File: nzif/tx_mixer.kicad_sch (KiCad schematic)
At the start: 51 parts, among them U143 SN74CBT3125CPW, U144 SN74CBT3125CPW, U145 SN74CBT3125CPW, U146 SN74CBT3125CPW, U147 ADG918BRM, U148 ADA4807-2ACP, U149 ADA4807-2ACP, U150 ADA4807-2ACP, U151 ADG918BRM

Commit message: Digikey parts for rcv stages
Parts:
- C292, C293, C294, C295: Digikey Part # (none) -> 587-3258-1-ND
- C296, C297, C298, C299: Digikey Part # (none) -> 490-GCM31C5C1H104FA16LCT-ND
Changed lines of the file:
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@@
 			)
 		)
-		(property "Datasheet" "~"
+		(property "Datasheet" "https://search.murata.co.jp/Ceramy/image/img/A01X/G101/ENG/GCM31C5C1H104FA16-01.pdf"
 			(at 55.88 26.67 0)
 			(effects
@@
 			)
 		)
-		(property "Digikey Part #" ""
+		(property "Digikey Part #" "490-GCM31C5C1H104FA16LCT-ND"
 			(at 55.88 26.67 0)
 			(effects
@@
 			)
 		)
-		(property "Datasheet" "~"
+		(property "Datasheet" "https://search.murata.co.jp/Ceramy/image/img/A01X/G101/ENG/GCM31C5C1H104FA16-01.pdf"
 			(at 55.88 153.67 0)
 			(effects
@@
 			)
 		)
-		(property "Digikey Part #" ""
+		(property "Digikey Part #" "490-GCM31C5C1H104FA16LCT-ND"
 			(at 55.88 153.67 0)
 			(effects
@@
 			)
 		)
-		(property "Datasheet" "~"
+		(property "Datasheet" "https://search.murata.co.jp/Ceramy/image/img/A01X/G101/ENG/GCM31C5C1H104FA16-01.pdf"
 			(at 55.88 217.17 0)
 			(effects
@@
 			)
 		)
-		(property "Digikey Part #" ""
+		(property "Digikey Part #" "490-GCM31C5C1H104FA16LCT-ND"
 			(at 55.88 217.17 0)
 			(effects
@@
 			)
 		)
-		(property "Datasheet" "~"
+		(property "Datasheet" "https://mm.digikey.com/Volume0/opasdata/d220001/medias/docus/1231/LMK107BBJ106MALT_SS.pdf"
 			(at 46.99 90.17 0)
 			(effects
@@
 			)
 		)
-		(property "Digikey Part #" ""
+		(property "Digikey Part #" "587-3258-1-ND"
 			(at 46.99 90.17 0)
 			(effects
@@
 			)
 		)
-		(property "Datasheet" "~"
+		(property "Datasheet" "https://mm.digikey.com/Volume0/opasdata/d220001/medias/docus/1231/LMK107BBJ106MALT_SS.pdf"
 			(at 46.99 153.67 0)
 			(effects
@@
 			)
 		)
-		(property "Digikey Part #" ""
+		(property "Digikey Part #" "587-3258-1-ND"
 			(at 46.99 153.67 0)
 			(effects
@@
 			)
 		)
-		(property "Datasheet" "~"
+		(property "Datasheet" "https://search.murata.co.jp/Ceramy/image/img/A01X/G101/ENG/GCM31C5C1H104FA16-01.pdf"
 			(at 55.88 90.17 0)
 			(effects
@@
 			)
 		)
-		(property "Digikey Part #" ""
+		(property "Digikey Part #" "490-GCM31C5C1H104FA16LCT-ND"
 			(at 55.88 90.17 0)
 			(effects
@@
 			)
 		)
-		(property "Datasheet" "~"
+		(property "Datasheet" "https://mm.digikey.com/Volume0/opasdata/d220001/medias/docus/1231/LMK107BBJ106MALT_SS.pdf"
 			(at 46.99 217.17 0)
 			(effects
@@
 			)
 		)
-		(property "Digikey Part #" ""
+		(property "Digikey Part #" "587-3258-1-ND"
 			(at 46.99 217.17 0)
 			(effects
@@
 			)
 		)
-		(property "Datasheet" "~"
+		(property "Datasheet" "https://mm.digikey.com/Volume0/opasdata/d220001/medias/docus/1231/LMK107BBJ106MALT_SS.pdf"
 			(at 46.99 26.67 0)
 			(effects
@@
 			)
 		)
-		(property "Digikey Part #" ""
+		(property "Digikey Part #" "587-3258-1-ND"
 			(at 46.99 26.67 0)
 			(effects

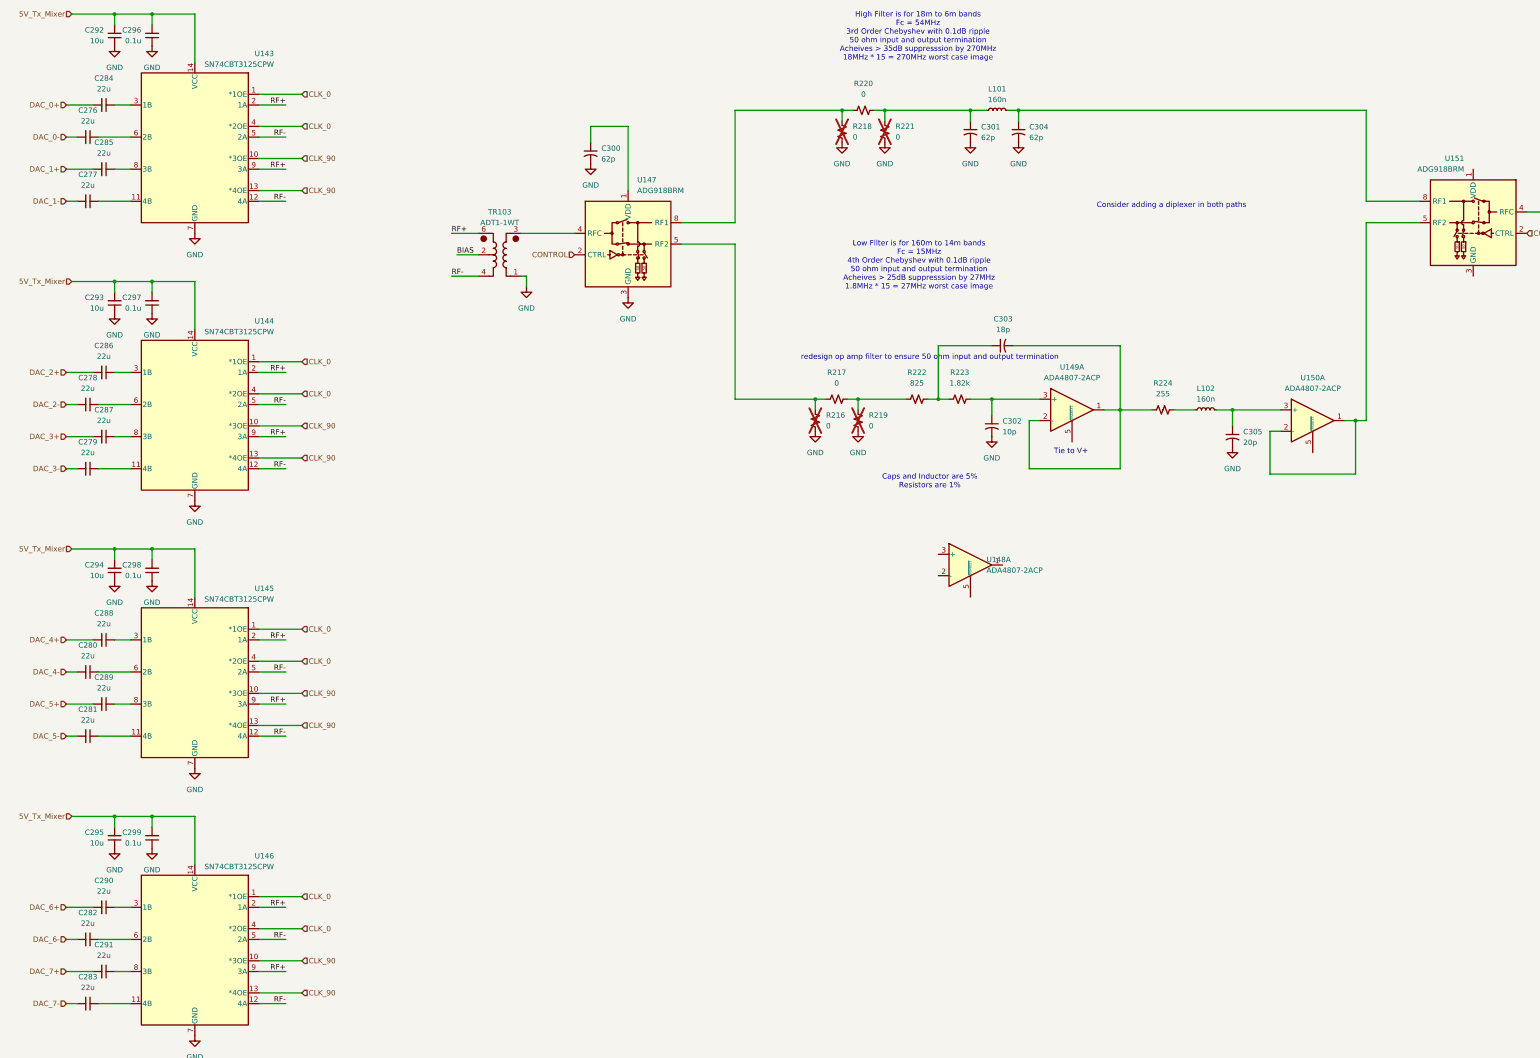
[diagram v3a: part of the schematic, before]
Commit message: add annotations - first run of erc
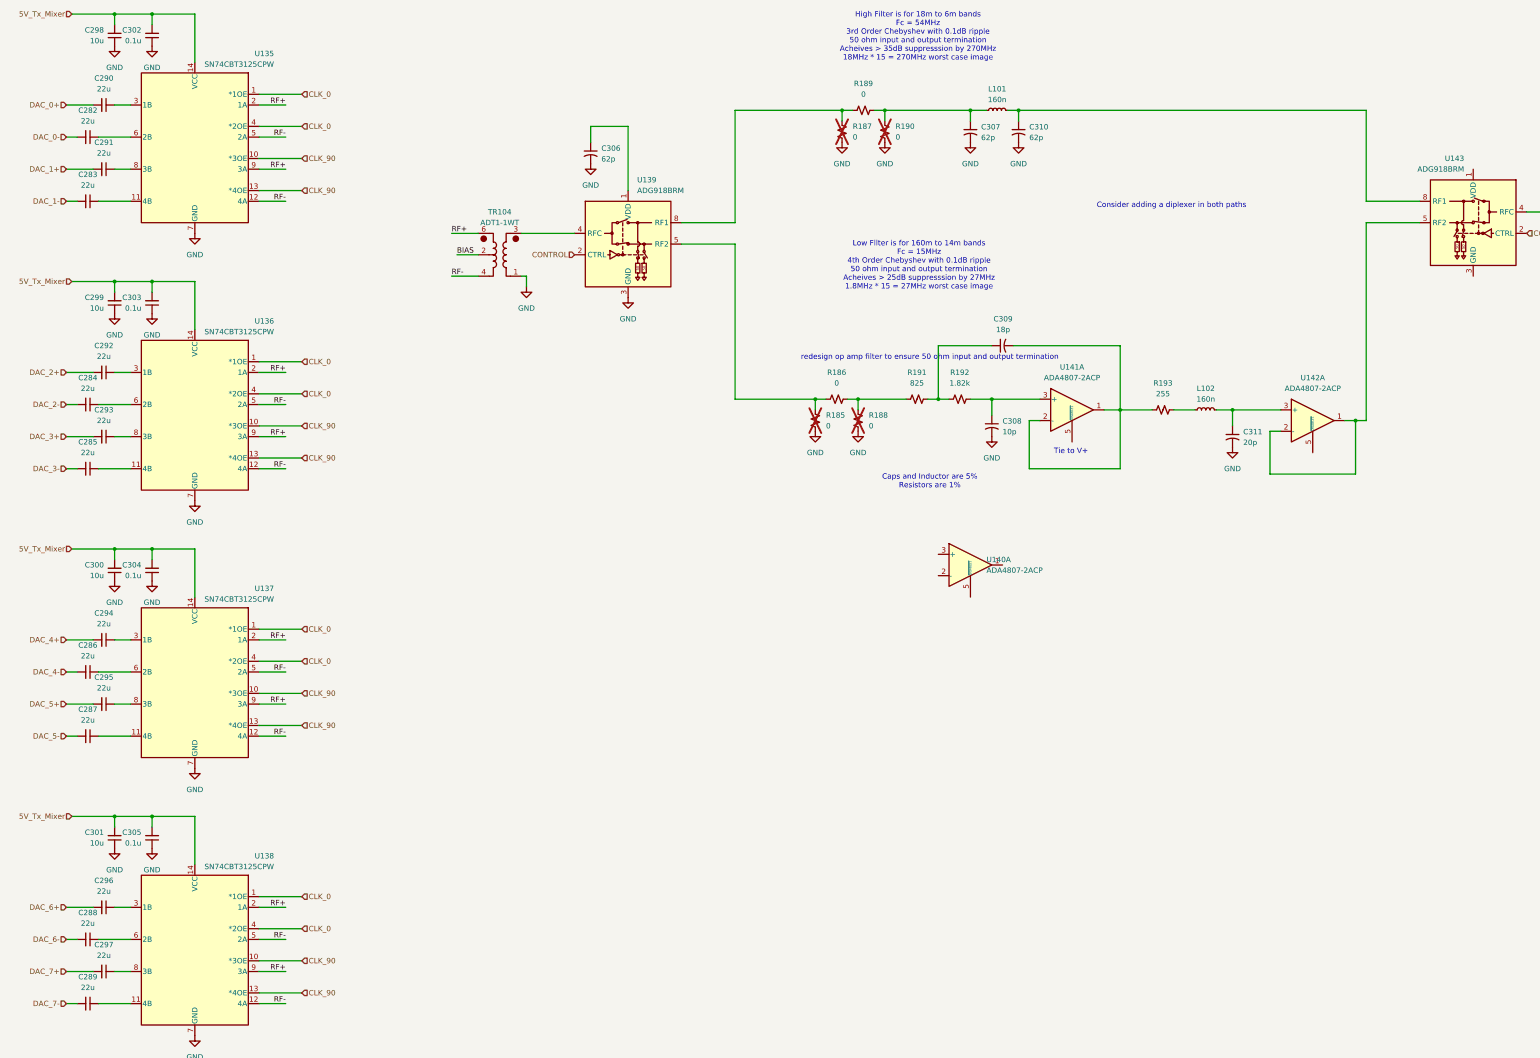
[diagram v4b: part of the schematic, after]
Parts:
- renumbered C276 to C282, C277 to C283, C278 to C284, C279 to C285, C280 to C286, C281 to C287, C282 to C288, C283 to C289, C284 to C290, C285 to C291, C286 to C292, C287 to C293, C288 to C294, C289 to C295, C290 to C296, C291 to C297, C292 to C298, C293 to C299, C294 to C300, C295 to C301, C296 to C302, C297 to C303, C298 to C304, C299 to C305, C300 to C306, C301 to C307, C302 to C308, C303 to C309, C304 to C310, C305 to C311, R216 to R185, R217 to R186, R218 to R187, R219 to R188, R220 to R189, R221 to R190, R222 to R191, R223 to R192, R224 to R193, TR103 to TR104, U143 to U135, U144 to U136, U145 to U137, U146 to U138, U147 to U139, U148 to U140, U149 to U141, U150 to U142, U151 to U143

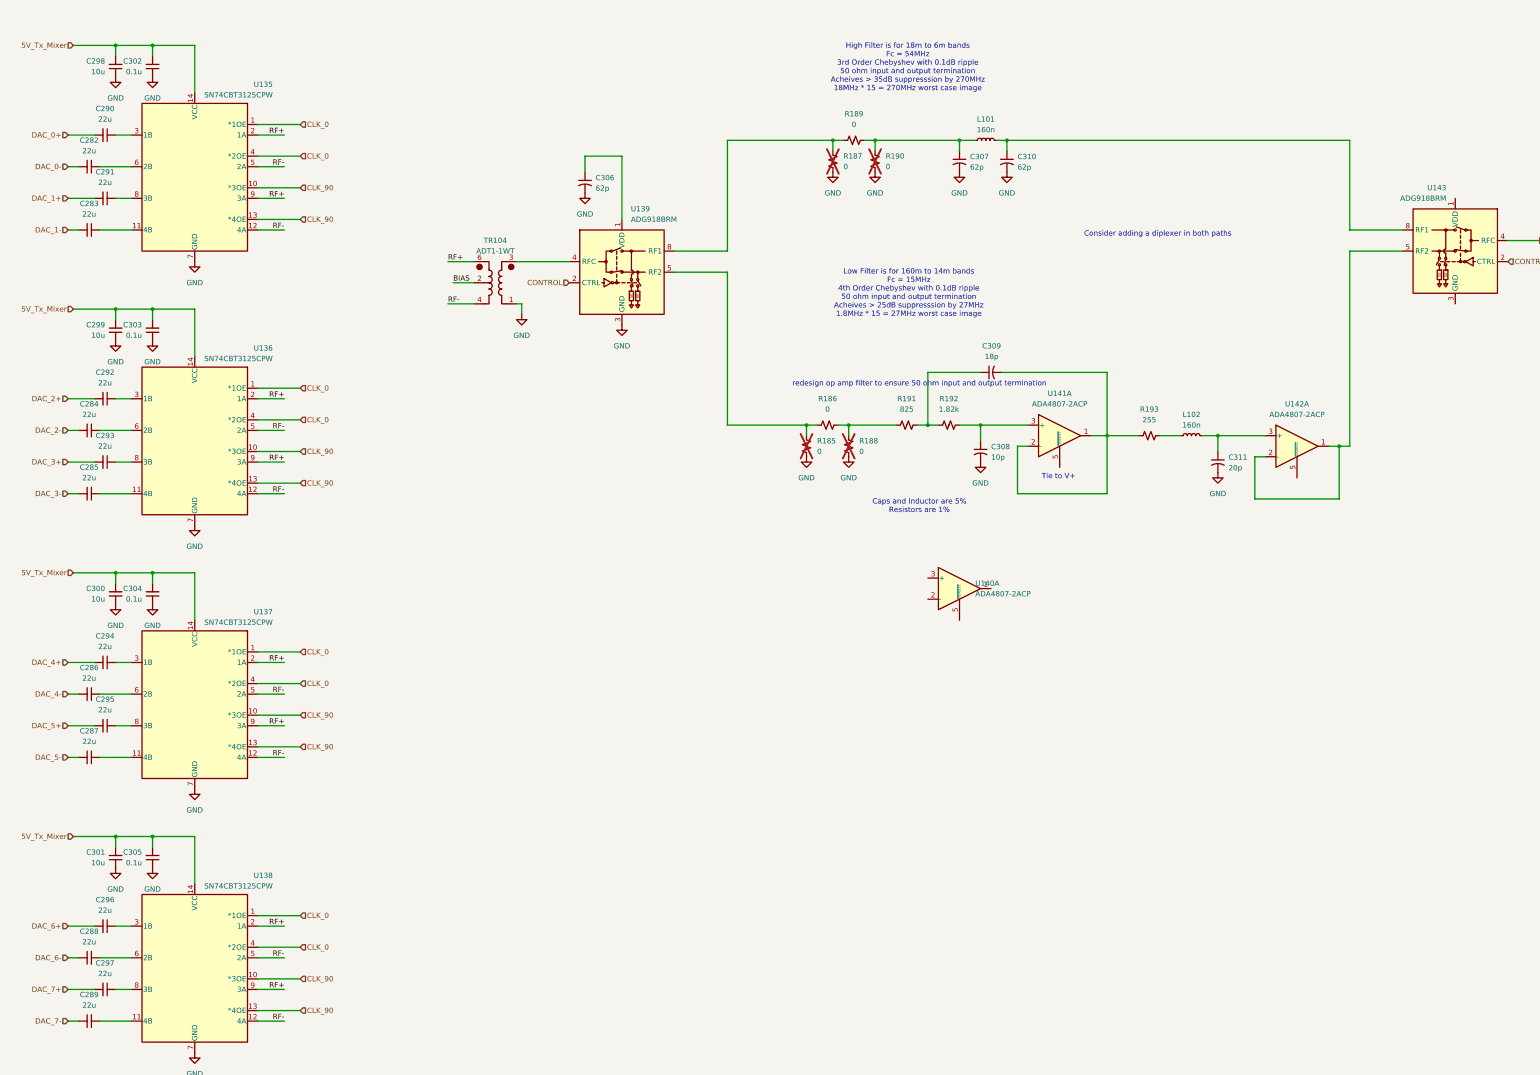
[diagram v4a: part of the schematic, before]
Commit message: updated power on all schematics
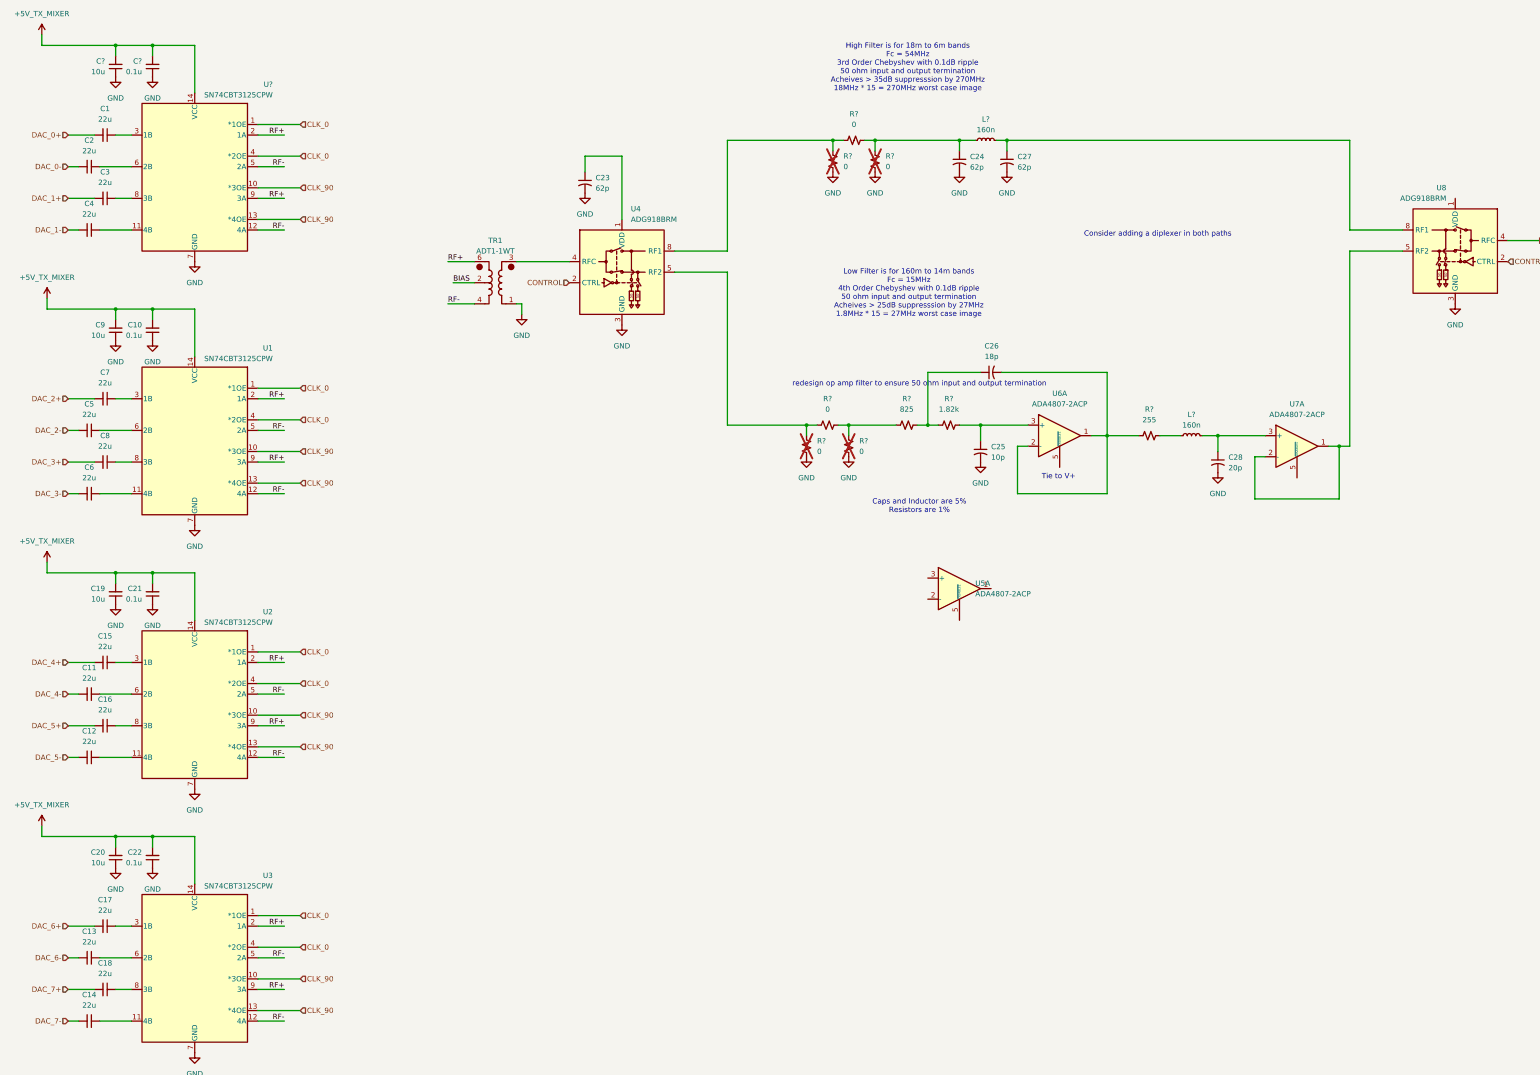
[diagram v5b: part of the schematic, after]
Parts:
- renumbered C290 to C1, C303 to C10, C286 to C11, C287 to C12, C288 to C13, C289 to C14, C294 to C15, C295 to C16, C296 to C17, C297 to C18, C300 to C19, C282 to C2, C301 to C20, C304 to C21, C305 to C22, C306 to C23, C307 to C24, C308 to C25, C309 to C26, C310 to C27, C311 to C28, C291 to C3, C283 to C4, C284 to C5, C285 to C6, C292 to C7, C293 to C8, C299 to C9, C302 to C?, C298 to C?, L101 to L?, L102 to L?, R185 to R?, R188 to R?, R187 to R?, R193 to R?, R186 to R?, R190 to R?, R189 to R?, R191 to R?, R192 to R?, TR104 to TR1, U136 to U1, U137 to U2, U138 to U3, U139 to U4, U140 to U5, U141 to U6, U142 to U7, U143 to U8, U135 to U?
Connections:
- net GND: now also U8.3 (GND), U8.6 (GND), U8.7 (GND)
- net 5V_Tx_Mixer renamed +5V_TX_MIXER

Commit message: fixed the tx mixer to align to dac outputs
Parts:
- removed C23, C24, C27: 62p, symbol Device:C_Small_US
- removed C25: 10p, symbol Device:C_Small_US
- removed C26: 18p, symbol Device:C_Small_US
- removed C28: 20p, symbol Device:C_Small_US
- removed L? (x2): 160n, symbol Device:L_Small
- removed R? (x6): 0, symbol Device:R_Small_US
- removed R?: 255, symbol Device:R_Small_US
- removed R?: 825, symbol Device:R_Small_US
- removed R?: 1.82k, symbol Device:R_Small_US
- removed TR1: ADT1-1WT, RF_Mini-Circuits:Mini-Circuits_CD542_H2.84mm, symbol Transformer:ADT1-1WT
- removed U4, U8: ADG918BRM, Package_SO:MSOP-8_3x3mm_P0.65mm, symbol RF_Switch:ADG918BRM
- removed U5, U6, U7: ADA4807-2ACP, Package_CSP:LFCSP-WD-10-1EP_3x3mm_P0.5mm_EP1.64x2.38mm, symbol Amplifier_Operational:ADA4807-2ACP
- C1, C11, C12, C13, C14, C15, C16, C17, C18, C2, C3, C4, C5, C6, C7, C8: value 22u -> 100n
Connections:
- net CLK_0: no longer U1.1 (*1OE), U1.4 (*2OE), U2.1 (*1OE), U2.4 (*2OE), U3.1 (*1OE), U3.4 (*2OE)
- net CLK_90: now also U2.1 (*1OE), U2.4 (*2OE); no longer U1.10 (*3OE), U1.13 (*4OE), U2.10 (*3OE), U2.13 (*4OE), U3.10 (*3OE), U3.13 (*4OE), U?.10 (*3OE), U?.13 (*4OE)
- net DAC_1+ renamed DAC_180+
- net DAC_1- renamed DAC_180-
- net DAC_2+ renamed DAC_45+
- net DAC_2- renamed DAC_45-
- net DAC_3+ renamed DAC_225+
- net DAC_3- renamed DAC_225-
- net DAC_4+ renamed DAC_90+
- net DAC_4- renamed DAC_90-
- net DAC_5+ renamed DAC_270+
- net DAC_5- renamed DAC_270-
- net DAC_6+ renamed DAC_135+
- net DAC_6- renamed DAC_135-
- net DAC_7+ renamed DAC_315+
- net DAC_7- renamed DAC_315-
- new net CLK_135: U3.1 (*1OE), U3.4 (*2OE)
- new net CLK_180: U?.10 (*3OE), U?.13 (*4OE)
- new net CLK_225: U1.10 (*3OE), U1.13 (*4OE)
- new net CLK_270: U2.10 (*3OE), U2.13 (*4OE)
- new net CLK_315: U3.10 (*3OE), U3.13 (*4OE)
- new net CLK_45: U1.1 (*1OE), U1.4 (*2OE)
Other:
- note removed: "Caps and Inductor are 5% Resistors are 1%"
- note removed: "Consider adding a diplexer in both paths"
- note removed: "High Filter is for 18m to 6m bands Fc = 54MHz 3rd Order Chebyshev with 0.1dB ripple 50 ohm input and output termination Acheives > 35dB suppresssion by 270MHz 18MHz * 15 = 270MHz worst case image"
- note removed: "Low Filter is for 160m to 14m bands Fc = 15MHz 4th Order Chebyshev with 0.1dB ripple 50 ohm input and output termination Acheives > 25dB suppresssion by 27MHz 1.8MHz * 15 = 27MHz worst case image"
- note removed: "Tie to V+"
- note removed: "redesign op amp filter to ensure 50 ohm input and output termination"
- moved on the sheet: C1, C10, C11, C12, C13, C14, C15, C16, C17, C18, C19, C2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
